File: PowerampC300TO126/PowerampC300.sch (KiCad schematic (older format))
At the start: 123 parts, among them J1 Conn_01x02, J2 Conn_01x02, J3 Conn_01x02, J4 Conn_01x01, J5 Conn_01x01, J6 Conn_01x01, J7 Conn_01x01, J8 Conn_01x02, J9 Conn_Coaxial, Q1 2N5551, Q10 MJE350, Q11 MJE340, Q12 MJE340, Q13 2N5551, Q14 2N5401, Q15 MJE340, Q16 MJE350, Q17 MJL3281A, Q18 MJL1302A, Q19 MJL3281A, Q2 2N5551, Q20 MJL1302A, Q21 MJL3281A, Q22 MJL1302A, Q23 MJL3281A, Q24 MJL1302A, Q3 2N5401, Q4 2N5401, Q5 2N5551, Q6 2N5551, Q7 2N5551, Q8 2N5401

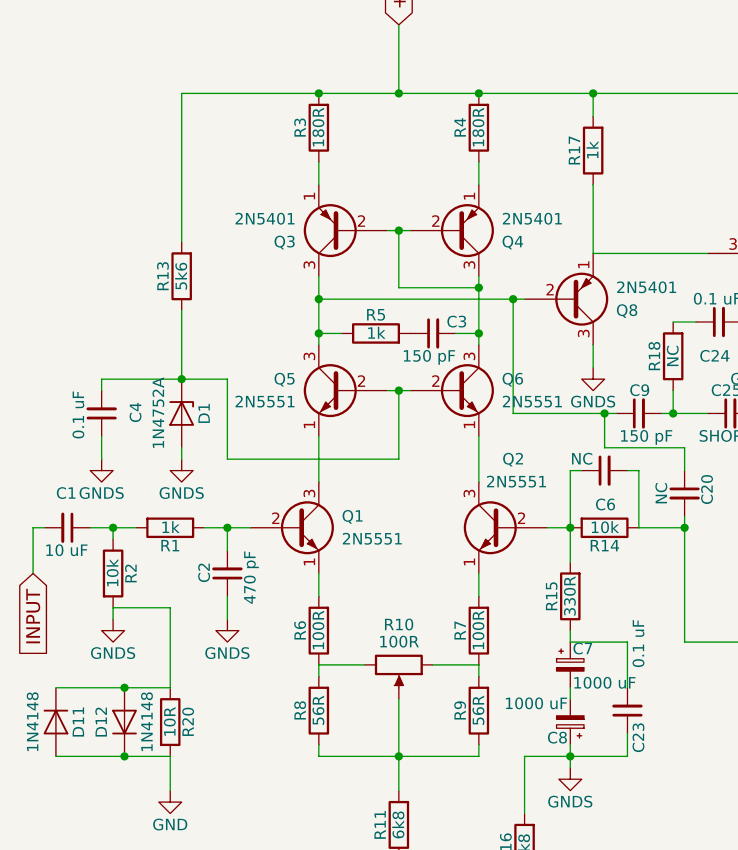
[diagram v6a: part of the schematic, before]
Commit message: Additions of optional zener diodes to limit current surges
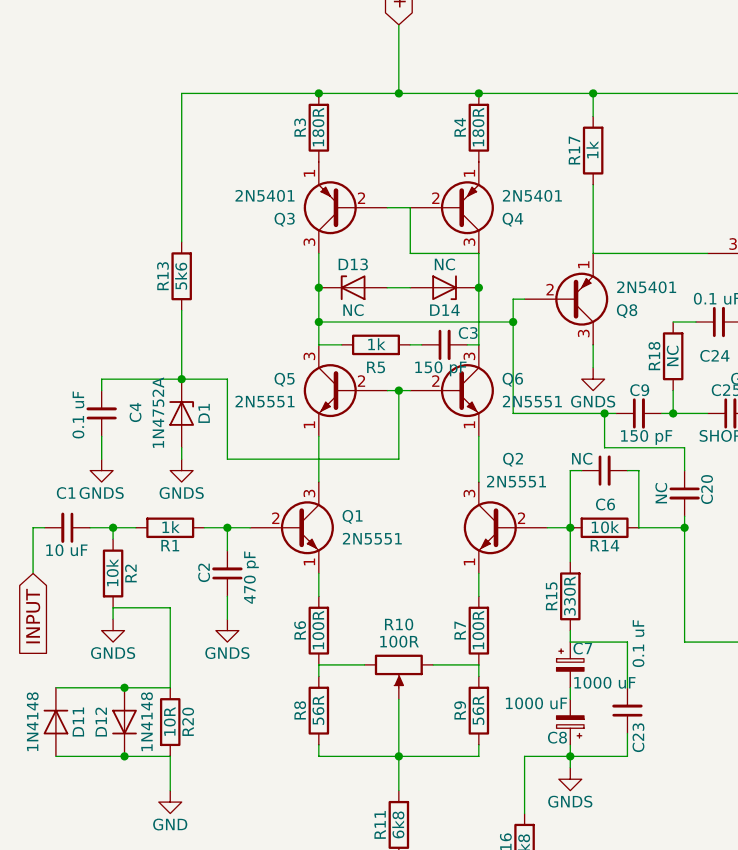
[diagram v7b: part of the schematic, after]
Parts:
- added D13, D14: NC, Diodes_THT:D_DO-41_SOD81_P7.62mm_Horizontal, symbol D_Zener
- C2: footprint Capacitors_THT:C_Axial_L3.8mm_D2.6mm_P7.50mm_Horizontal -> Capacitors_THT:C_Rect_L7.0mm_W3.5mm_P5.00mm
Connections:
- net at C20.1, C9.1, Q3.3 (C)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: now also D13.1 (K)
- net at C3.2, Q3.2 (B), Q4.2 (B)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: now also D14.1 (K)
- new net: D13.2 (A), D14.2 (A)
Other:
- moved on the sheet: C3, Q3, Q4, R5
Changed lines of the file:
@@
 F 0 "C2" V 1600 3850 50  0000 L CNN
 F 1 "470 pF" V 1400 3800 50  0000 L CNN
-F 2 "Capacitors_THT:C_Axial_L3.8mm_D2.6mm_P7.50mm_Horizontal" H 1500 3900 50  0001 C CNN
+F 2 "Capacitors_THT:C_Rect_L7.0mm_W3.5mm_P5.00mm" H 1500 3900 50  0001 C CNN
 F 3 "" H 1500 3900 50  0001 C CNN
 F 4 "C328872" V 1500 3900 60  0001 C CNN "LCSC"
@@
 $EndComp
 $Comp
-L GND #PWR01
+L GND #PWR3
 U 1 1 5F3B09D1
 P 1250 4850
-F 0 "#PWR01" H 1250 4600 50  0001 C CNN
+F 0 "#PWR3" H 1250 4600 50  0001 C CNN
 F 1 "GND" H 1250 4700 50  0000 C CNN
 F 2 "" H 1250 4850 50  0001 C CNN
@@
 L R R5
 U 1 1 5F3B2121
-P 2150 2850
-F 0 "R5" V 2230 2850 50  0000 C CNN
-F 1 "1k" V 2150 2850 50  0000 C CNN
-F 2 "Resistors_THT:R_Axial_DIN0207_L6.3mm_D2.5mm_P7.62mm_Horizontal" V 2080 2850 50  0001 C CNN
-F 3 "" H 2150 2850 50  0001 C CNN
-F 4 "C173036" V 2150 2850 60  0001 C CNN "LCSC"
-	1    2150 2850
+P 2150 2900
+F 0 "R5" V 2050 2900 50  0000 C CNN
+F 1 "1k" V 2150 2900 50  0000 C CNN
+F 2 "Resistors_THT:R_Axial_DIN0207_L6.3mm_D2.5mm_P7.62mm_Horizontal" V 2080 2900 50  0001 C CNN
+F 3 "" H 2150 2900 50  0001 C CNN
+F 4 "C173036" V 2150 2900 60  0001 C CNN "LCSC"
+	1    2150 2900
 	0    -1   -1   0
 $EndComp
@@
 L C_Small C3
 U 1 1 5F3B2238
-P 2400 2850
-F 0 "C3" V 2450 2700 50  0000 L CNN
-F 1 "150 pF" V 2300 2750 50  0000 L CNN
-F 2 "Capacitors_THT:C_Axial_L3.8mm_D2.6mm_P7.50mm_Horizontal" H 2400 2850 50  0001 C CNN
-F 3 "" H 2400 2850 50  0001 C CNN
-F 4 "C434407" V 2400 2850 60  0001 C CNN "LCSC"
-	1    2400 2850
+P 2450 2900
+F 0 "C3" V 2500 2750 50  0000 L CNN
+F 1 "150 pF" V 2350 2800 50  0000 L CNN
+F 2 "Capacitors_THT:C_Axial_L3.8mm_D2.6mm_P7.50mm_Horizontal" H 2450 2900 50  0001 C CNN
+F 3 "" H 2450 2900 50  0001 C CNN
+F 4 "C434407" V 2450 2900 60  0001 C CNN "LCSC"
+	1    2450 2900
 	0    -1   -1   0
 $EndComp
@@
 $EndComp
 $Comp
-L GND #PWR02
+L GND #PWR13
 U 1 1 5F3C725A
 P 9450 4900
-F 0 "#PWR02" H 9450 4650 50  0001 C CNN
+F 0 "#PWR13" H 9450 4650 50  0001 C CNN
 F 1 "GND" H 9450 4750 50  0000 C CNN
 F 2 "" H 9450 4900 50  0001 C CNN
@@
 $EndComp
 $Comp
-L GND #PWR03
+L GND #PWR12
 U 1 1 5F3C82FF
 P 9150 6100
-F 0 "#PWR03" H 9150 5850 50  0001 C CNN
+F 0 "#PWR12" H 9150 5850 50  0001 C CNN
 F 1 "GND" H 9150 5950 50  0000 C CNN
 F 2 "" H 9150 6100 50  0001 C CNN
@@
 $EndComp
 $Comp
-L GND #PWR04
+L GND #PWR11
 U 1 1 5F3C9FC4
 P 9100 2800
-F 0 "#PWR04" H 9100 2550 50  0001 C CNN
+F 0 "#PWR11" H 9100 2550 50  0001 C CNN
 F 1 "GND" H 9100 2650 50  0000 C CNN
 F 2 "" H 9100 2800 50  0001 C CNN
@@
 OUTPUT
 $Comp
-L GND #PWR05
+L GND #PWR17
 U 1 1 5F3D5C64
 P 10700 3450
-F 0 "#PWR05" H 10700 3200 50  0001 C CNN
+F 0 "#PWR17" H 10700 3200 50  0001 C CNN
 F 1 "GND" H 10700 3300 50  0000 C CNN
 F 2 "" H 10700 3450 50  0001 C CNN
@@
 $EndComp
 $Comp
-L GND #PWR06
+L GND #PWR16
 U 1 1 5F3D7497
 P 10650 5700
-F 0 "#PWR06" H 10650 5450 50  0001 C CNN
+F 0 "#PWR16" H 10650 5450 50  0001 C CNN
 F 1 "GND" H 10650 5550 50  0000 C CNN
 F 2 "" H 10650 5700 50  0001 C CNN
@@
 $EndComp
 $Comp
-L GND #PWR07
+L GND #PWR18
 U 1 1 5F3D76F6
 P 10800 5150
-F 0 "#PWR07" H 10800 4900 50  0001 C CNN
+F 0 "#PWR18" H 10800 4900 50  0001 C CNN
 F 1 "GND" H 10800 5000 50  0000 C CNN
 F 2 "" H 10800 5150 50  0001 C CNN
@@
 L Q_PNP_EBC Q4
 U 1 1 5F5DB1DC
-P 2500 2400
-F 0 "Q4" H 2700 2450 50  0000 L CNN
-F 1 "2N5401" H 2700 2350 50  0000 L CNN
-F 2 "TO_SOT_Packages_THT:TO-92_Inline_Wide" H 2700 2500 50  0001 C CNN
-F 3 "" H 2500 2400 50  0001 C CNN
-	1    2500 2400
+P 2500 2300
+F 0 "Q4" H 2700 2350 50  0000 L CNN
+F 1 "2N5401" H 2700 2250 50  0000 L CNN
+F 2 "TO_SOT_Packages_THT:TO-92_Inline_Wide" H 2700 2400 50  0001 C CNN
+F 3 "" H 2500 2300 50  0001 C CNN
+	1    2500 2300
 	1    0    0    1
 $EndComp
@@
 L Q_PNP_EBC Q3
 U 1 1 5F5DB57B
-P 2000 2400
-F 0 "Q3" H 2200 2450 50  0000 L CNN
-F 1 "2N5401" H 2200 2350 50  0000 L CNN
-F 2 "TO_SOT_Packages_THT:TO-92_Inline_Wide" H 2200 2500 50  0001 C CNN
-F 3 "" H 2000 2400 50  0001 C CNN
-	1    2000 2400
+P 2000 2300
+F 0 "Q3" H 2200 2350 50  0000 L CNN
+F 1 "2N5401" H 2200 2250 50  0000 L CNN
+F 2 "TO_SOT_Packages_THT:TO-92_Inline_Wide" H 2200 2400 50  0001 C CNN
+F 3 "" H 2000 2300 50  0001 C CNN
+	1    2000 2300
 	-1   0    0    1
 $EndComp
@@
 $EndComp
 $Comp
-L GND #PWR08
+L GND #PWR14
 U 1 1 5F83634A
 P 9850 4650
-F 0 "#PWR08" H 9850 4400 50  0001 C CNN
+F 0 "#PWR14" H 9850 4400 50  0001 C CNN
 F 1 "GND" H 9850 4500 50  0000 C CNN
 F 2 "" H 9850 4650 50  0001 C CNN
@@
 $EndComp
 $Comp
-L GNDS #PWR09
+L GNDS #PWR2
 U 1 1 5F90B752
 P 1000 4100
-F 0 "#PWR09" H 1000 3850 50  0001 C CNN
+F 0 "#PWR2" H 1000 3850 50  0001 C CNN
 F 1 "GNDS" H 1000 3950 50  0000 C CNN
 F 2 "" H 1000 4100 50  0001 C CNN
@@
 $EndComp
 $Comp
-L GNDS #PWR010
+L GNDS #PWR5
 U 1 1 5F90C0B2
 P 1500 4100
-F 0 "#PWR010" H 1500 3850 50  0001 C CNN
+F 0 "#PWR5" H 1500 3850 50  0001 C CNN
 F 1 "GNDS" H 1500 3950 50  0000 C CNN
 F 2 "" H 1500 4100 50  0001 C CNN
@@
 $EndComp
 $Comp
-L GNDS #PWR011
+L GNDS #PWR6
 U 1 1 5F90C20A
 P 3000 4750
-F 0 "#PWR011" H 3000 4500 50  0001 C CNN
+F 0 "#PWR6" H 3000 4500 50  0001 C CNN
 F 1 "GNDS" H 3000 4600 50  0000 C CNN
 F 2 "" H 3000 4750 50  0001 C CNN
@@
 $EndComp
 $Comp
-L GNDS #PWR012
+L GNDS #PWR8
 U 1 1 5F90CB3D
 P 3800 2900
-F 0 "#PWR012" H 3800 2650 50  0001 C CNN
+F 0 "#PWR8" H 3800 2650 50  0001 C CNN
 F 1 "GNDS" H 3800 2750 50  0000 C CNN
 F 2 "" H 3800 2900 50  0001 C CNN
@@
 $EndComp
 $Comp
-L GNDS #PWR013
+L GNDS #PWR1
 U 1 1 5F90D661
 P 950 3400
-F 0 "#PWR013" H 950 3150 50  0001 C CNN
+F 0 "#PWR1" H 950 3150 50  0001 C CNN
 F 1 "GNDS" H 950 3250 50  0000 C CNN
 F 2 "" H 950 3400 50  0001 C CNN
@@
 $EndComp
 $Comp
-L GNDS #PWR014
+L GNDS #PWR4
 U 1 1 5F90D829
 P 1300 3400
-F 0 "#PWR014" H 1300 3150 50  0001 C CNN
+F 0 "#PWR4" H 1300 3150 50  0001 C CNN
 F 1 "GNDS" H 1300 3250 50  0000 C CNN
 F 2 "" H 1300 3400 50  0001 C CNN
@@
 $EndComp
 $Comp
-L GNDS #PWR015
+L GNDS #PWR7
 U 1 1 5F90FE32
 P 3100 3000
-F 0 "#PWR015" H 3100 2750 50  0001 C CNN
+F 0 "#PWR7" H 3100 2750 50  0001 C CNN
 F 1 "GNDS" H 3100 2850 50  0000 C CNN
 F 2 "" H 3100 3000 50  0001 C CNN
@@
 $EndComp
 $Comp
-L GNDS #PWR016
+L GNDS #PWR15
 U 1 1 5F910AB2
 P 10500 2750
-F 0 "#PWR016" H 10500 2500 50  0001 C CNN
+F 0 "#PWR15" H 10500 2500 50  0001 C CNN
 F 1 "GNDS" H 10500 2600 50  0000 C CNN
 F 2 "" H 10500 2750 50  0001 C CNN
@@
 $EndComp
 $Comp
-L GNDS #PWR017
+L GNDS #PWR10
 U 1 1 5F911887
 P 8750 1200
-F 0 "#PWR017" H 8750 950 50  0001 C CNN
+F 0 "#PWR10" H 8750 950 50  0001 C CNN
 F 1 "GNDS" H 8750 1050 50  0000 C CNN
 F 2 "" H 8750 1200 50  0001 C CNN
@@
 $EndComp
 $Comp
-L GND #PWR018
+L GND #PWR9
 U 1 1 5F912230
 P 8750 850
-F 0 "#PWR018" H 8750 600 50  0001 C CNN
+F 0 "#PWR9" H 8750 600 50  0001 C CNN
 F 1 "GND" H 8750 700 50  0000 C CNN
 F 2 "" H 8750 850 50  0001 C CNN
@@
 Connection ~ 1300 3050
 Wire Wire Line
-	1900 2600 1900 2900
-Wire Wire Line
-	2600 2600 2600 2900
-Wire Wire Line
-	2200 2400 2300 2400
-Wire Wire Line
-	2250 2400 2250 2650
-Wire Wire Line
-	2250 2650 2600 2650
-Connection ~ 2600 2650
-Connection ~ 2250 2400
-Wire Wire Line
-	2600 2100 2600 2200
-Wire Wire Line
-	1900 2100 1900 2200
+	1900 2500 1900 2900
+Wire Wire Line
+	2600 2500 2600 2900
 Wire Wire Line
 	1300 2750 1300 3050
@@
 Connection ~ 3900 4650
 Wire Wire Line
-	2000 2850 1900 2850
-Connection ~ 1900 2850
-Wire Wire Line
-	2300 2850 2300 2850
-Wire Wire Line
-	2600 2850 2500 2850
-Connection ~ 2600 2850
-Wire Wire Line
-	1900 2700 2800 2700
-Connection ~ 1900 2700
+	2750 2700 2800 2700
 Wire Wire Line
 	3100 3000 3100 2900
@@
 Wire Wire Line
 	2750 2700 2750 3200
-Connection ~ 2750 2700
 Wire Wire Line
 	2600 3500 2600 3300
@@
 	1000 4050 1250 4050
 Wire Wire Line
-	1250 4050 1250 4400
+	1250 4400 1250 4050
 Wire Wire Line
 	1250 4700 1250 4850
 Wire Wire Line
-	1250 4400 750  4400
+	750  4400 1250 4400
 Wire Wire Line
 	750  4700 1250 4700
@@
 	1    0    0    -1
 $EndComp
+Wire Wire Line
+	2600 2900 2550 2900
+Wire Wire Line
+	1900 2900 2000 2900
+Wire Wire Line
+	1900 2800 2750 2800
+Connection ~ 2750 2800
+Connection ~ 1900 2800
+Wire Wire Line
+	2300 2300 2200 2300
+Wire Wire Line
+	2300 2300 2300 2500
+Wire Wire Line
+	2300 2500 2600 2500
+Wire Wire Line
+	2350 2900 2300 2900
+$Comp
+L D_Zener D13
+U 1 1 608C429E
+P 2050 2650
+F 0 "D13" H 2050 2750 50  0000 C CNN
+F 1 "NC" H 2050 2550 50  0000 C CNN
+F 2 "Diodes_THT:D_DO-41_SOD81_P7.62mm_Horizontal" H 2050 2650 50  0001 C CNN
+F 3 "" H 2050 2650 50  0001 C CNN
+F 4 "C2555" H 2050 2650 60  0001 C CNN "LCSC"
+	1    2050 2650
+	1    0    0    -1
+$EndComp
+$Comp
+L D_Zener D14
+U 1 1 608C45C4
+P 2450 2650
+F 0 "D14" H 2450 2750 50  0000 C CNN
+F 1 "NC" H 2450 2550 50  0000 C CNN
+F 2 "Diodes_THT:D_DO-41_SOD81_P7.62mm_Horizontal" H 2450 2650 50  0001 C CNN
+F 3 "" H 2450 2650 50  0001 C CNN
+F 4 "C2555" H 2450 2650 60  0001 C CNN "LCSC"
+	1    2450 2650
+	-1   0    0    1
+$EndComp
+Connection ~ 2600 2650
+Wire Wire Line
+	1900 2650 1900 2650
+Connection ~ 1900 2650
+Wire Wire Line
+	2300 2650 2200 2650
 $EndSCHEMATC

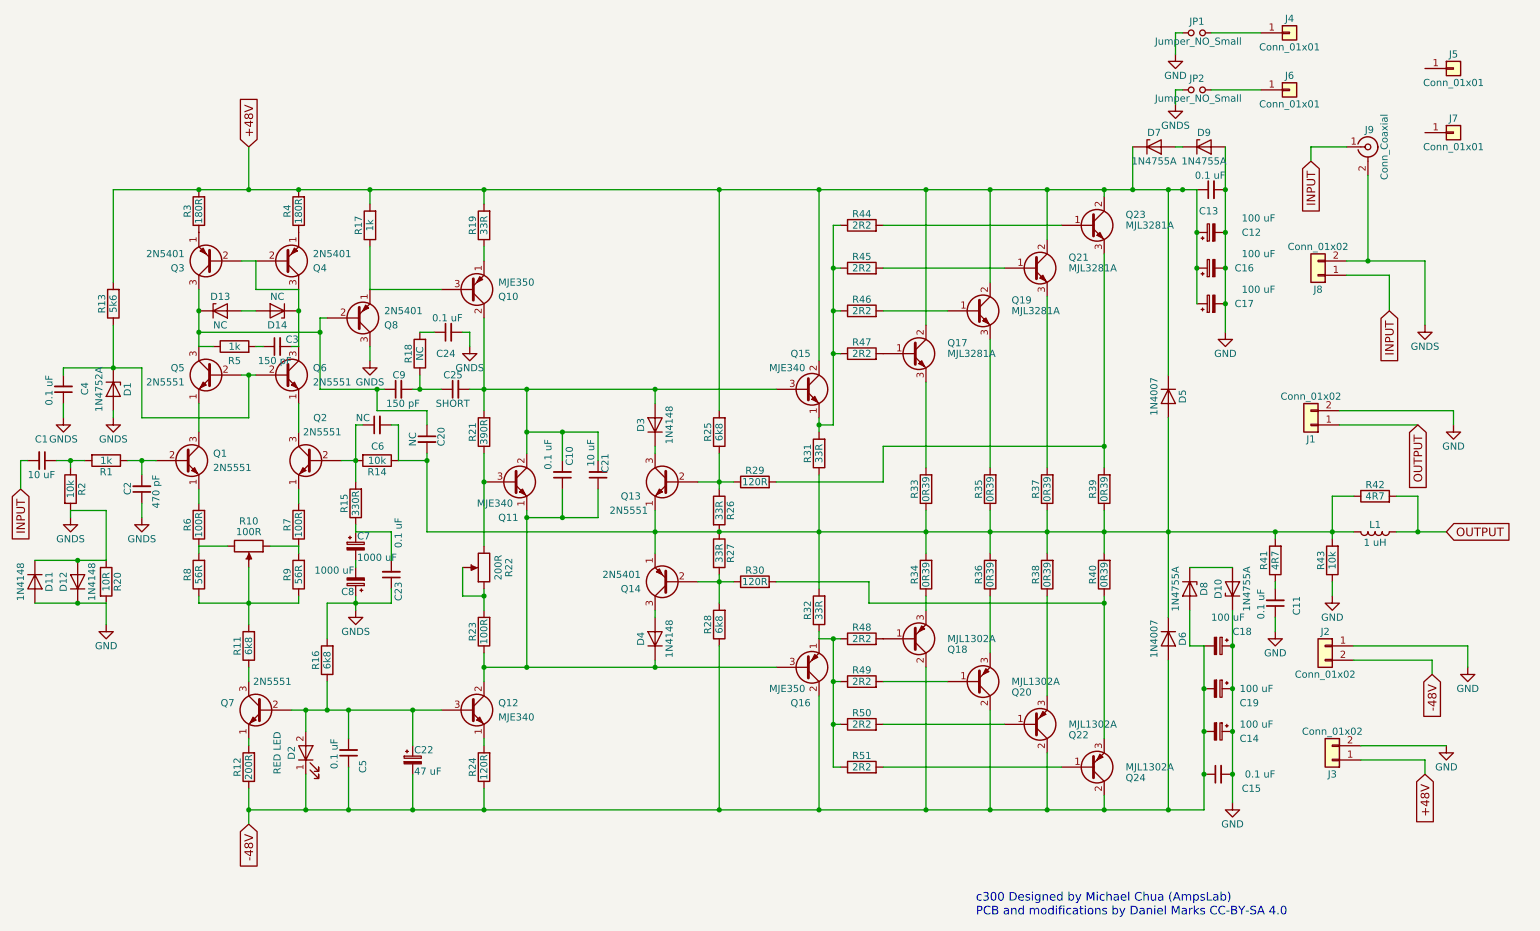
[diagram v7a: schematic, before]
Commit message: Changed to use optotriac shutoff of bias
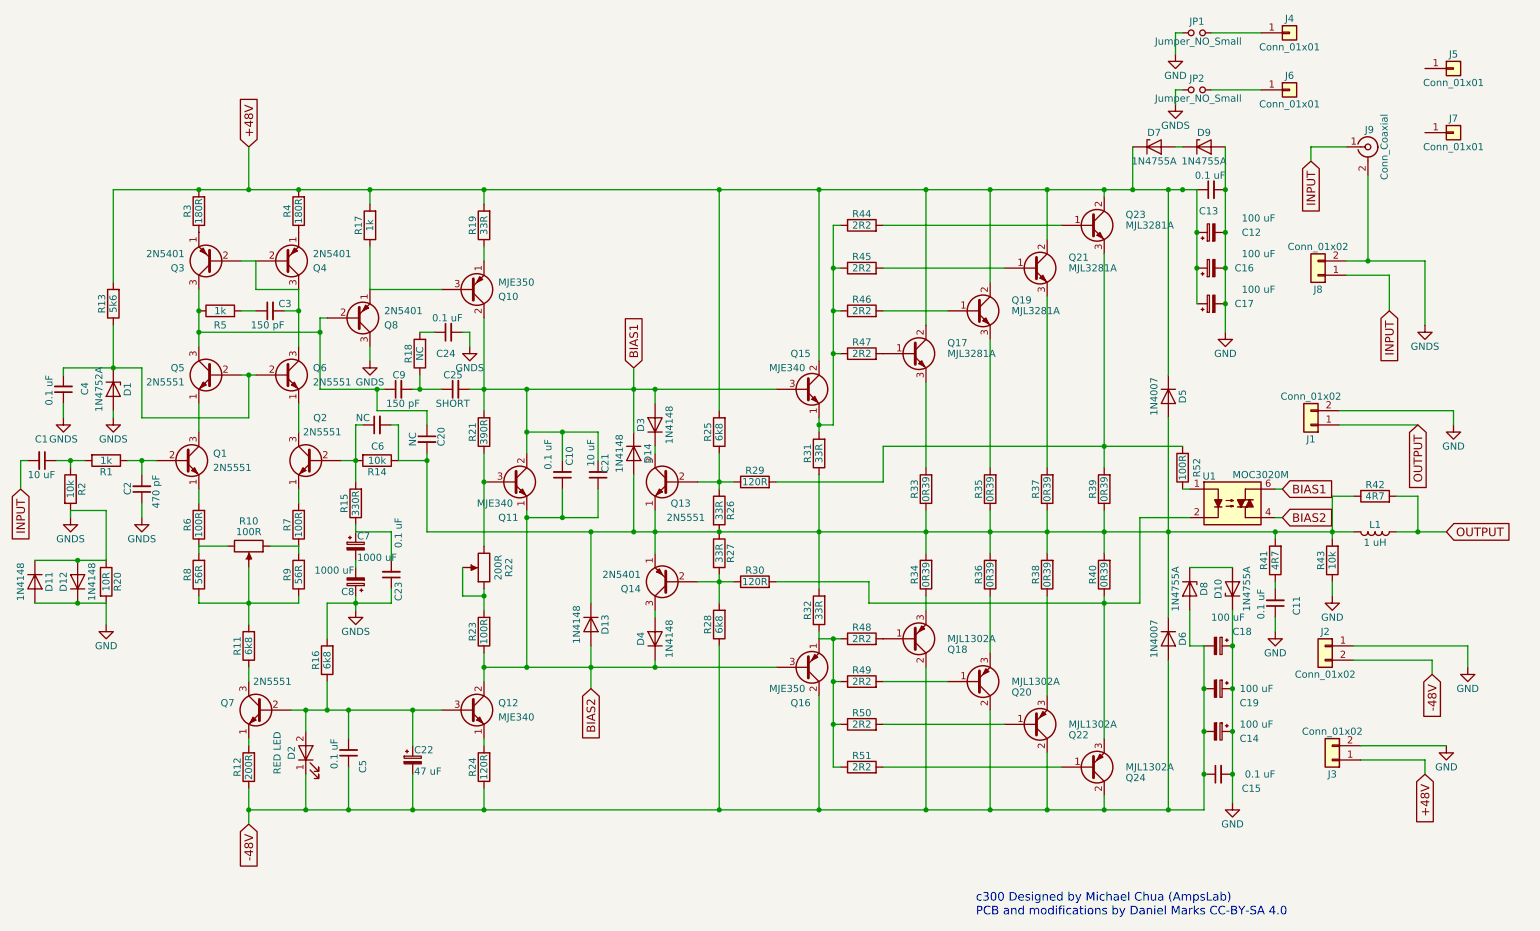
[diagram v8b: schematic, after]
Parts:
- removed D13, D14: NC, Diodes_THT:D_DO-41_SOD81_P7.62mm_Horizontal, symbol D_Zener
- added D13, D14: 1N4148, Diodes_THT:D_DO-35_SOD27_P7.62mm_Horizontal, symbol D
- added R52: 100R, Resistors_THT:R_Axial_DIN0207_L6.3mm_D2.5mm_P7.62mm_Horizontal, symbol R
- added U1: MOC3020M, Housings_DIP:DIP-6_W7.62mm, symbol MOC3020M
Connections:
- net at C20.2, C6.2, D5.2 (A)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: now also D13.1 (K), D14.2 (A)
- net BIAS2: now reaches C10.1, C21.1, D4.1 (K), Q11.1 (E), Q12.2 (C), Q16.3 (B), R23.1
- net BIAS2: now also D13.2 (A), U1.4
- net BIAS1: now reaches C10.2, C21.2, C25.2, D3.2 (A), Q10.2 (C), Q11.2 (C), Q15.3 (B), R21.2
- net BIAS1: now also D14.1 (K), U1.6
- net at Q23.3 (E), R29.2, R39.2: now also R52.2
- net at Q24.3 (E), R30.2, R40.1: now also U1.2
- new net: R52.1, U1.1
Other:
- moved on the sheet: C3, R5
